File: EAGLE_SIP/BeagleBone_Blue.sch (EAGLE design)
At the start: 276 parts, among them M1 JST_ZH_2, M2 JST_ZH_2, M3 JST_ZH_2, M4 JST_ZH_2, P10 SCHA5B0200, Q3 MOSFET-N, U1 TPD4S012_DRY_6, U4 TPD4S012_DRY_6, U5 24LC_32AT-I/OT, U6 SN74LVC1G07_DCK_5, U7 TPS2051B_D_8, U8 MTFC4GLDEA, Y1 CM200C-32.768KAZF-UT, Y2 445C33D24M00000

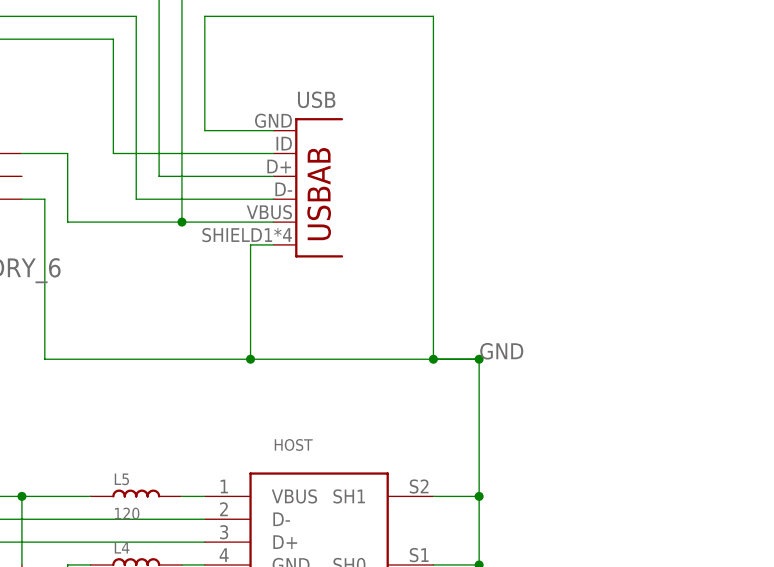
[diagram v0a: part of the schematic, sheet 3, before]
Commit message: ERC: add USB value
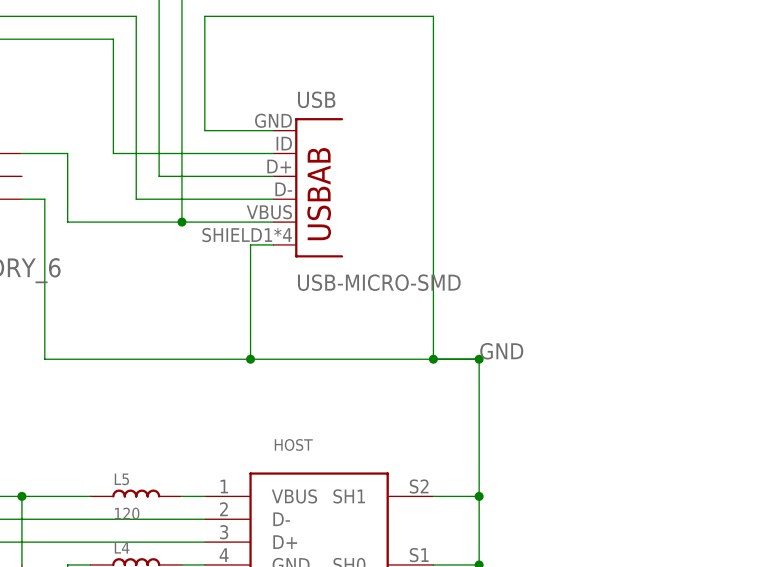
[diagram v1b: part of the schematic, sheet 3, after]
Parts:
- USB: value (none) -> USB-MICRO-SMD
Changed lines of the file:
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@@
 <part name="R158" library="Strawson_Eagle_Lib" deviceset="RESISTOR" device="0402-RES" value="10K,1%"/>
 <part name="5VREG" library="BeagleBone_Blue" deviceset="AP1509" device="SOIC-8-TIGHT" value="AP1509SOIC-8-TIGHT"/>
-<part name="USB" library="Strawson_Eagle_Lib" deviceset="USB-AB" device=""/>
+<part name="USB" library="Strawson_Eagle_Lib" deviceset="USB-AB" device="" value="USB-MICRO-SMD"/>
 </parts>
 <sheets>

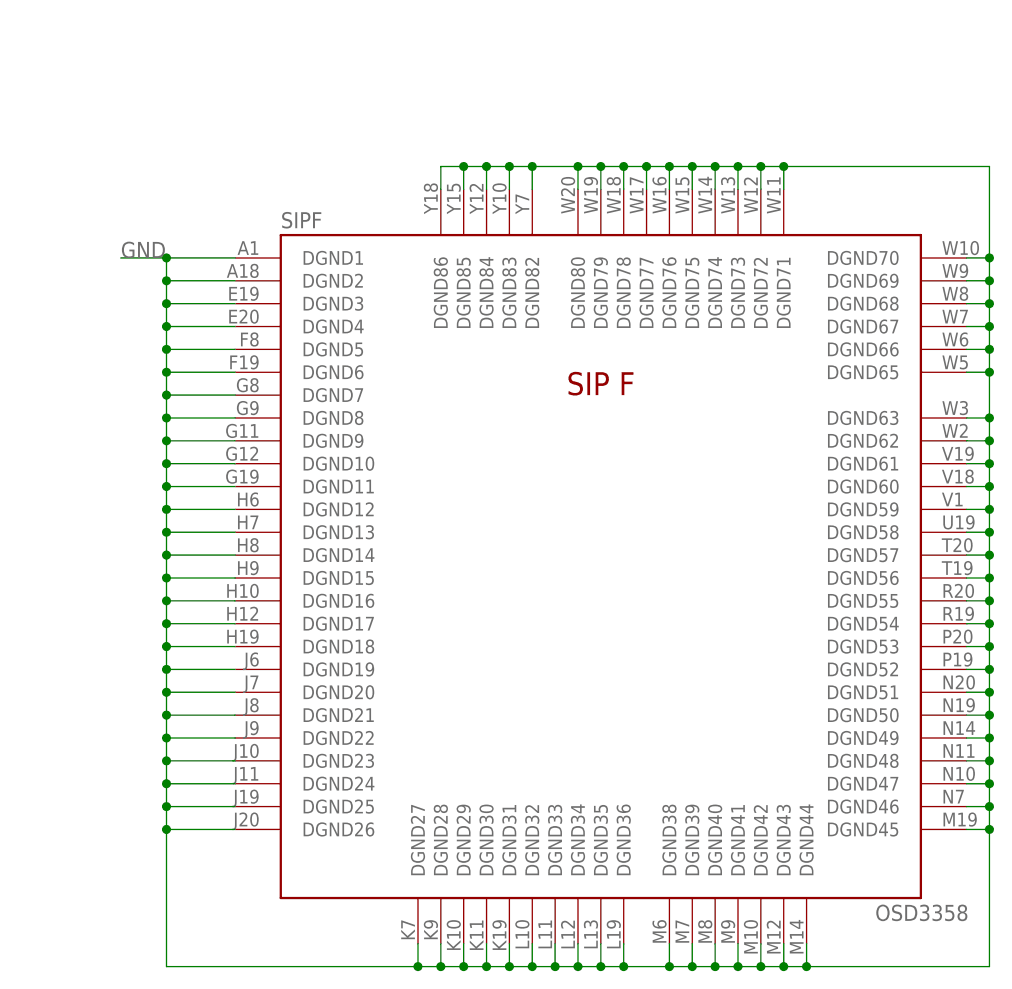
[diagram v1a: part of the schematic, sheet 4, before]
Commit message: Remove a bunch of redudnant grounds
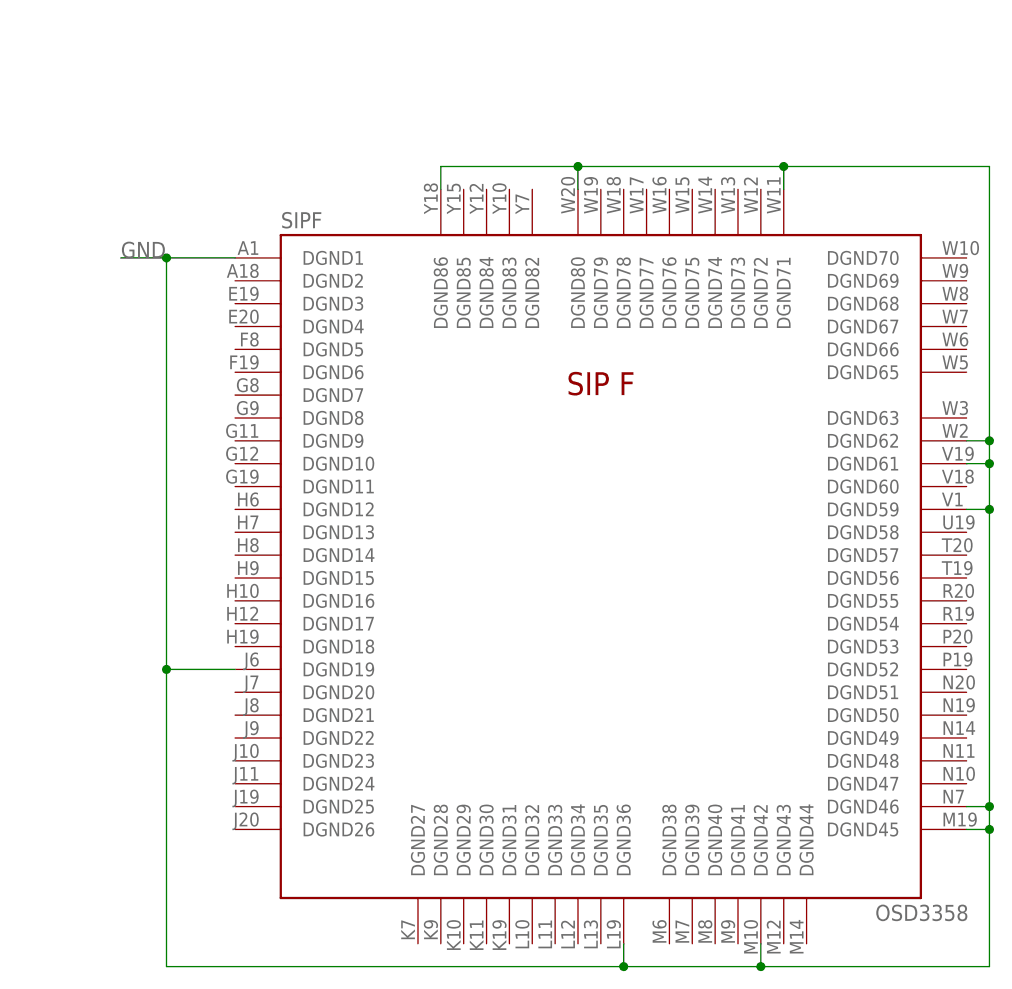
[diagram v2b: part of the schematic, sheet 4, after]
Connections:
- net GND: no longer SIPF.DGND10, SIPF.DGND11, SIPF.DGND12, SIPF.DGND13, SIPF.DGND14, SIPF.DGND15, SIPF.DGND16, SIPF.DGND17, SIPF.DGND18, SIPF.DGND2, SIPF.DGND20, SIPF.DGND21, SIPF.DGND22, SIPF.DGND23, SIPF.DGND24, SIPF.DGND25, SIPF.DGND26, SIPF.DGND27, SIPF.DGND28, SIPF.DGND29, SIPF.DGND3, SIPF.DGND30, SIPF.DGND31, SIPF.DGND32, SIPF.DGND33, SIPF.DGND34, SIPF.DGND35, SIPF.DGND38, SIPF.DGND39, SIPF.DGND4, SIPF.DGND40, SIPF.DGND41, SIPF.DGND43, SIPF.DGND44, SIPF.DGND47, SIPF.DGND48, SIPF.DGND49, SIPF.DGND5, SIPF.DGND50, SIPF.DGND51, SIPF.DGND52, SIPF.DGND53, SIPF.DGND54, SIPF.DGND55, SIPF.DGND56, SIPF.DGND57, SIPF.DGND58, SIPF.DGND6, SIPF.DGND60, SIPF.DGND63, SIPF.DGND65, SIPF.DGND66, SIPF.DGND67, SIPF.DGND68, SIPF.DGND69, SIPF.DGND7, SIPF.DGND70, SIPF.DGND72, SIPF.DGND73, SIPF.DGND74, SIPF.DGND75, SIPF.DGND76, SIPF.DGND77, SIPF.DGND78, SIPF.DGND79, SIPF.DGND8, SIPF.DGND82, SIPF.DGND83, SIPF.DGND84, SIPF.DGND85, SIPF.DGND9

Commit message: Fix VCC
CHGIC VIN was connected to "5.0V", not VCC.
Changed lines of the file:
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@@
 <part name="SUPPLY5" library="SparkFun-Aesthetics" deviceset="V_BATT" device=""/>
 <part name="V_DC" library="Strawson_Eagle_Lib" deviceset="VDC" device=""/>
-<part name="VCC" library="Strawson_Eagle_Lib" deviceset="VDC" device=""/>
 <part name="LIPO" library="Strawson_Eagle_Lib" deviceset="JST_XH_3-PIN" device=""/>
 <part name="DSM2" library="Strawson_Eagle_Lib" deviceset="JST_ZH_3" device="SMD_TOP"/>
@@
 <attribute name="VALUE" x="151.384" y="135.636" size="1.778" layer="96"/>
 </instance>
-<instance part="VCC" gate="G$1" x="214.63" y="248.92"/>
 <instance part="LIPO" gate="G$1" x="300.99" y="133.35" smashed="yes">
 <attribute name="NAME" x="297.18" y="137.16" size="1.778" layer="96"/>
@@
 </segment>
 <segment>
+<pinref part="SUPPLY1" gate="G$1" pin="VCC"/>
+<pinref part="R1" gate="G$1" pin="1"/>
+<wire x1="115.57" y1="41.91" x2="115.57" y2="40.64" width="0.1524" layer="91"/>
+</segment>
+<segment>
 <wire x1="214.63" y1="223.52" x2="214.63" y2="245.11" width="0.1524" layer="91"/>
 <wire x1="199.39" y1="245.11" x2="214.63" y2="245.11" width="0.1524" layer="91"/>
@@
 <pinref part="C12" gate="G$1" pin="1"/>
 <wire x1="226.06" y1="245.11" x2="214.63" y2="245.11" width="0.1524" layer="91"/>
-<wire x1="214.63" y1="248.92" x2="214.63" y2="245.11" width="0.1524" layer="91"/>
-<pinref part="VCC" gate="G$1" pin="VCC"/>
 <junction x="214.63" y="245.11"/>
 <pinref part="CHGIC" gate="G$1" pin="VIN"/>
@@
 <label x="200.66" y="245.11" size="1.778" layer="95"/>
 </segment>
-<segment>
-<pinref part="SUPPLY1" gate="G$1" pin="VCC"/>
-<pinref part="R1" gate="G$1" pin="1"/>
-<wire x1="115.57" y1="41.91" x2="115.57" y2="40.64" width="0.1524" layer="91"/>
-</segment>
-</net>
+</net>

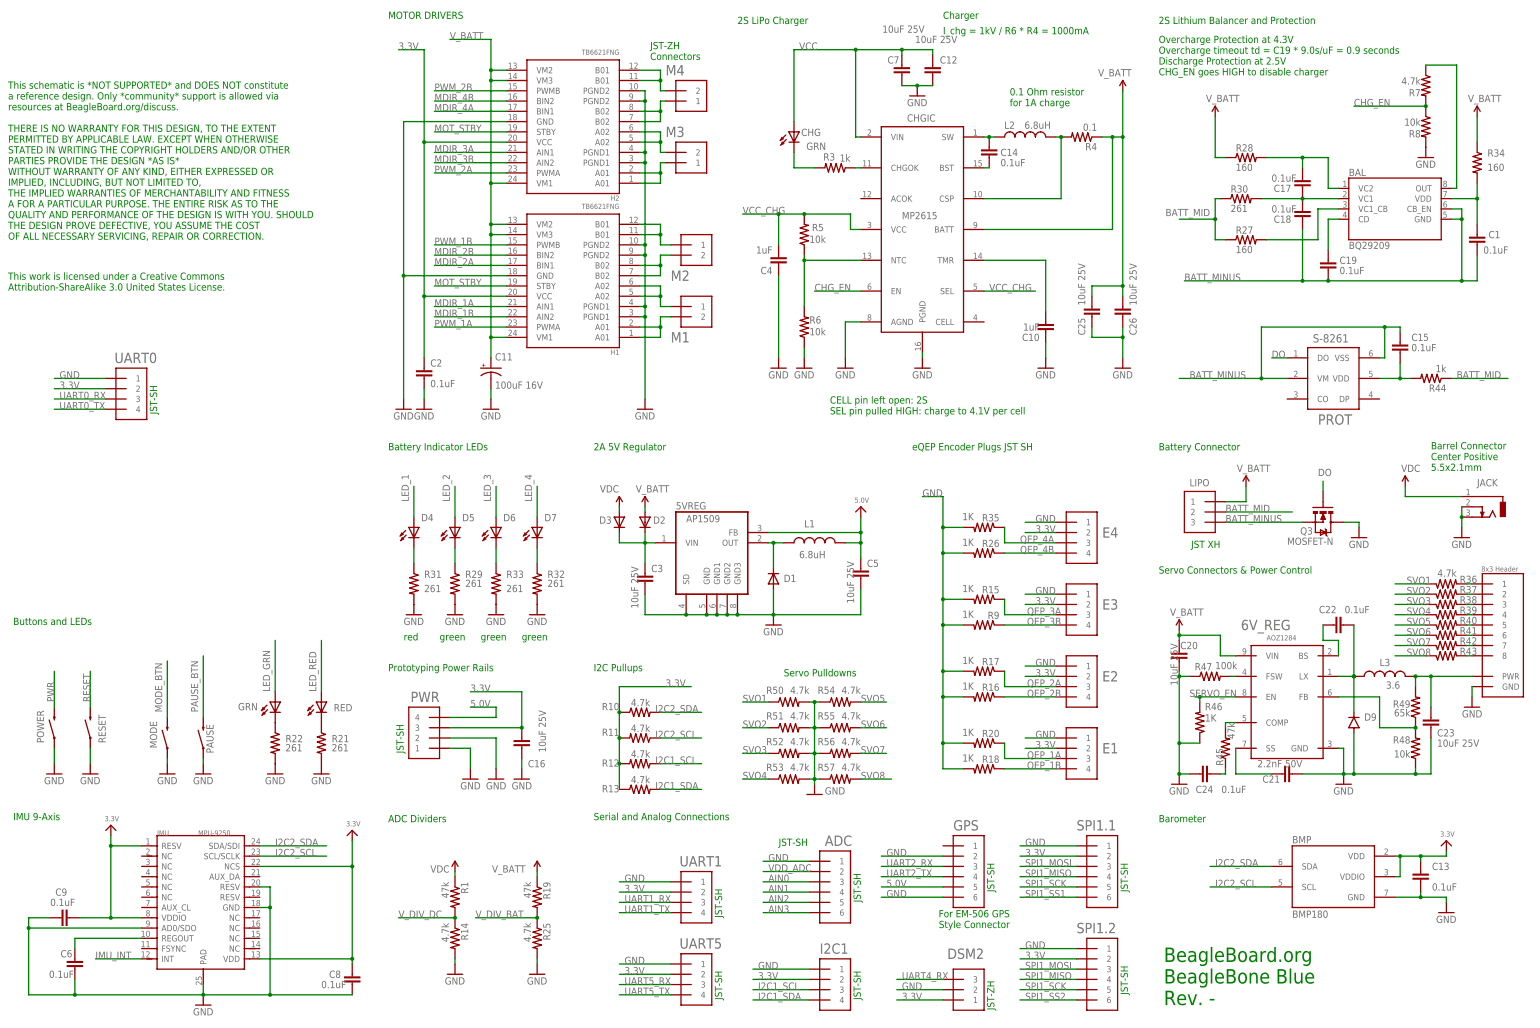
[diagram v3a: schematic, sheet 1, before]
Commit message: Remove unpredictable ports
Used labels and net names rather than power ports
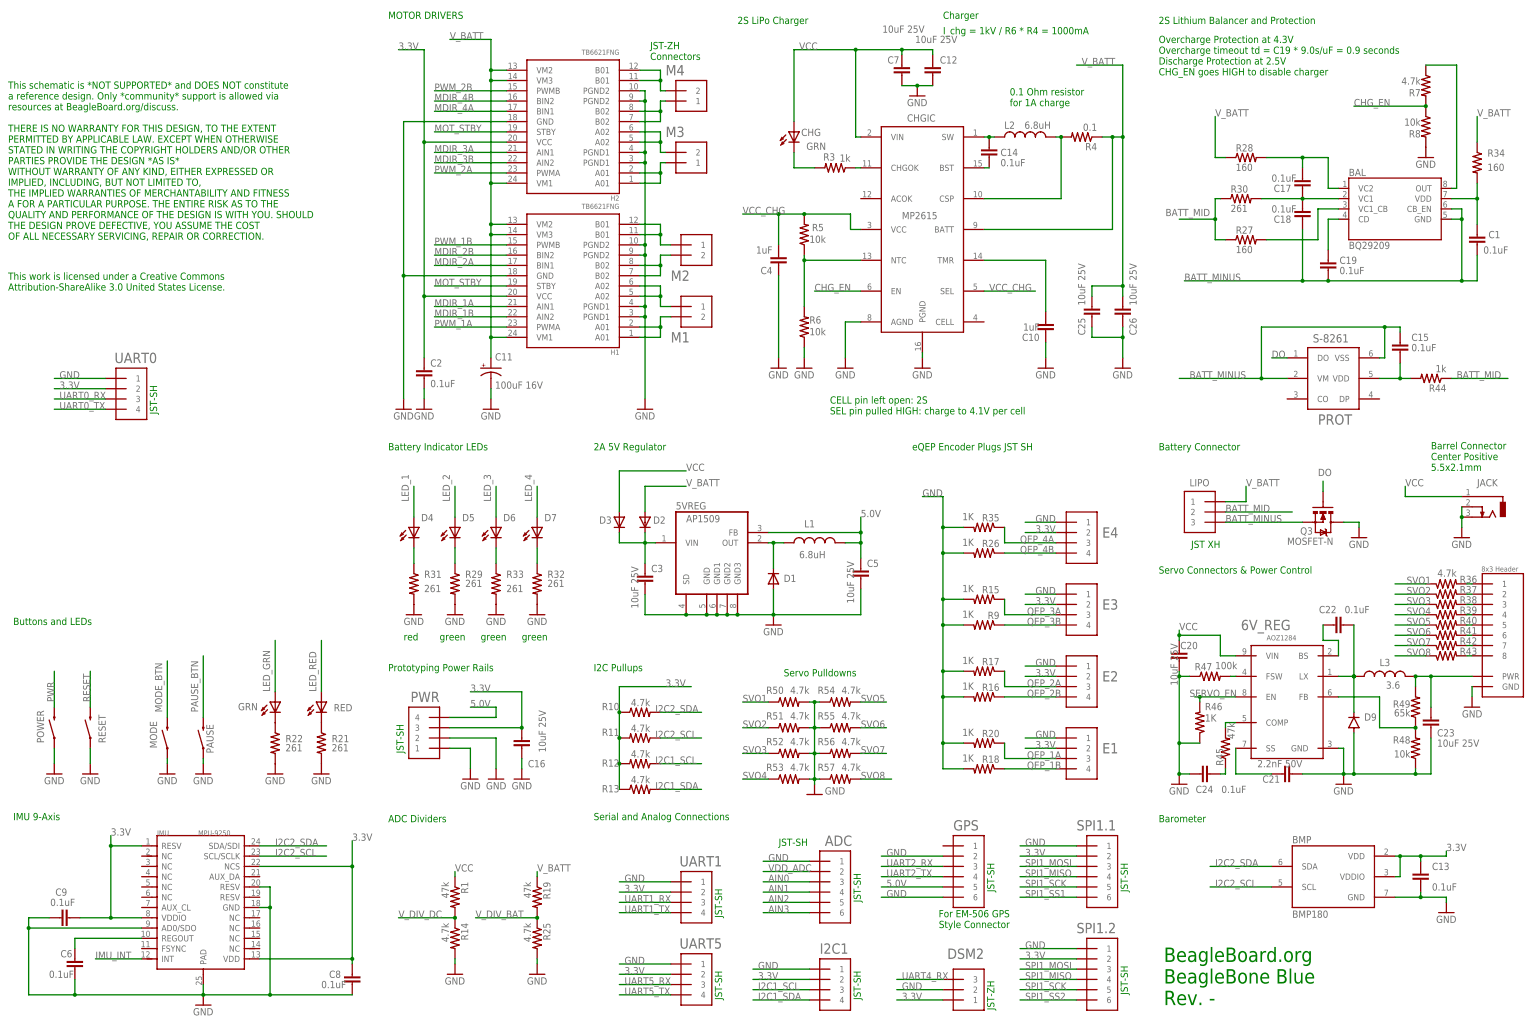
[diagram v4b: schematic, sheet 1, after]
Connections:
- net VCC: now also 6V_REG.VIN, C20.2
- net V_BATT: no longer 6V_REG.VIN, C20.2

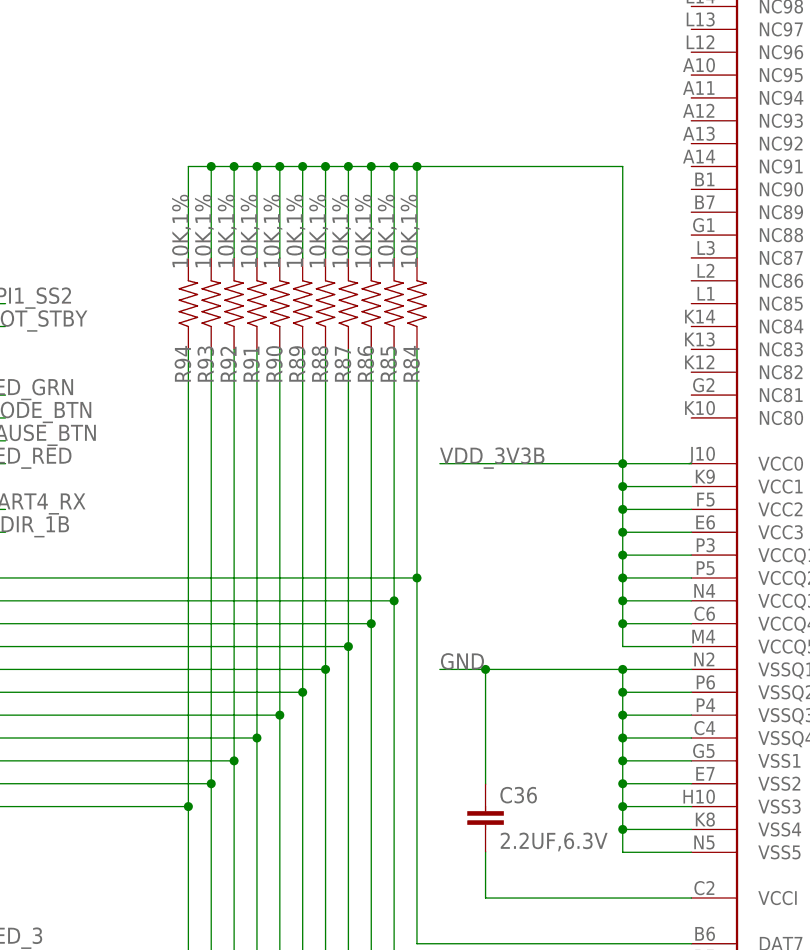
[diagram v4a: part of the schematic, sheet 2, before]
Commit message: eMMC pull-ups
CMD/CLK are pulled up internally by AM335x on reset.

DATx are pulled down internally by AM335x on reset and are push-pull in
operation.
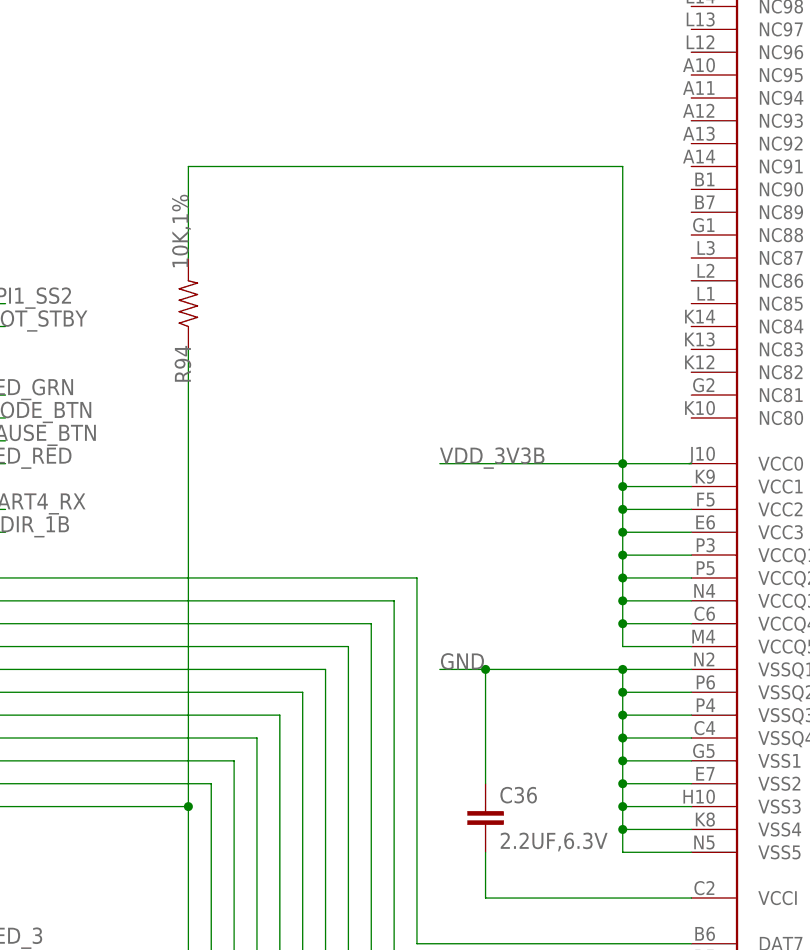
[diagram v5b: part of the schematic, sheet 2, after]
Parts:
- removed R84, R85, R86, R87, R88, R89, R90, R91, R92, R93: 10K,1%, Strawson_Eagle_Lib:RESISTOR0402-RES
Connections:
- net N$88: no longer R84.1
- net N$89: no longer R85.1
- net N$90: no longer R86.1
- net N$91: no longer R87.1
- net N$92: no longer R88.1
- net N$93: no longer R89.1
- net N$94: no longer R90.1
- net N$95: no longer R91.1
- net N$96: no longer R92.1
- net N$97: no longer R93.1
- net VDD_3V3B: no longer R84.2, R85.2, R86.2, R87.2, R88.2, R89.2, R90.2, R91.2, R92.2, R93.2
